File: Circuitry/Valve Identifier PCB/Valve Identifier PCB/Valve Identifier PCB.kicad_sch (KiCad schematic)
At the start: 34 parts

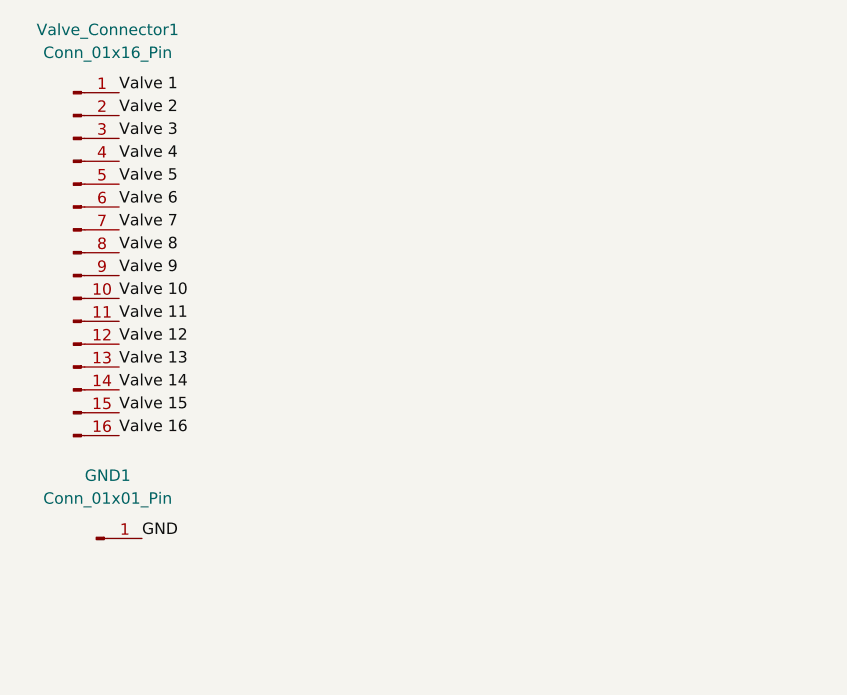
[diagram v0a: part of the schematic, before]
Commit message: add new mainboard design, led breakout board design kicad
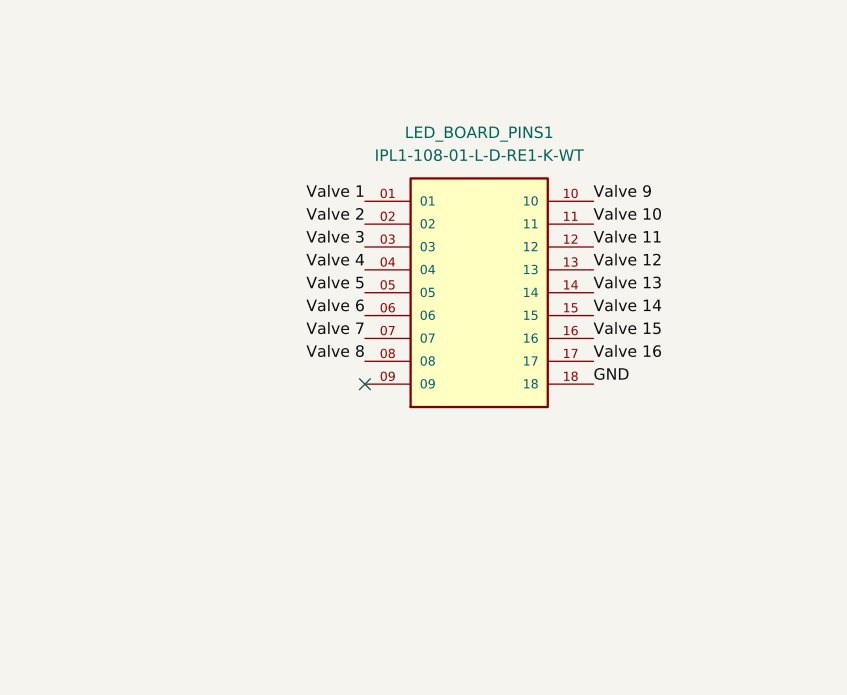
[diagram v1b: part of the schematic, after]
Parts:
- removed GND1: Conn_01x01_Pin, Connector_PinHeader_1.00mm:PinHeader_1x01_P1.00mm_Vertical, symbol Connector:Conn_01x01_Pin
- removed Valve_Connector1: Conn_01x16_Pin, Connector_PinHeader_1.00mm:PinHeader_1x16_P1.00mm_Vertical, symbol Connector:Conn_01x16_Pin
- added LED_BOARD_PINS1: IPL1-108-01-L-D-RE1-K-WT, IPL1-109-01-L-D-RE1-K:SAMTEC_IPL1-109-01-L-D-RE1-K, symbol IPL1-109-01-L-D-RE1-K:IPL1-109-01-L-D-RE1-K
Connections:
- net GND: now also LED_BOARD_PINS1.18
- net Valve 1: now also LED_BOARD_PINS1.01
- net Valve 10: now also LED_BOARD_PINS1.11
- net Valve 11: now also LED_BOARD_PINS1.12
- net Valve 12: now also LED_BOARD_PINS1.13
- net Valve 13: now also LED_BOARD_PINS1.14
- net Valve 14: now also LED_BOARD_PINS1.15
- net Valve 15: now also LED_BOARD_PINS1.16
- net Valve 16: now also LED_BOARD_PINS1.17
- net Valve 2: now also LED_BOARD_PINS1.02
- net Valve 3: now also LED_BOARD_PINS1.03
- net Valve 4: now also LED_BOARD_PINS1.04
- net Valve 5: now also LED_BOARD_PINS1.05
- net Valve 6: now also LED_BOARD_PINS1.06
- net Valve 7: now also LED_BOARD_PINS1.07
- net Valve 8: now also LED_BOARD_PINS1.08
- net Valve 9: now also LED_BOARD_PINS1.10
- no-connect marks 0 -> 1
